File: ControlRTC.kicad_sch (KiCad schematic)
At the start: 33 parts, among them M1 Fan_4pin, SW1 SW_USER, SW2 SW_WIPE, U18 74LVC1G07, U19 74LVC1G07, U20 LP5569RTWR, U21 PCF85063AT, Y2 X32K768S301

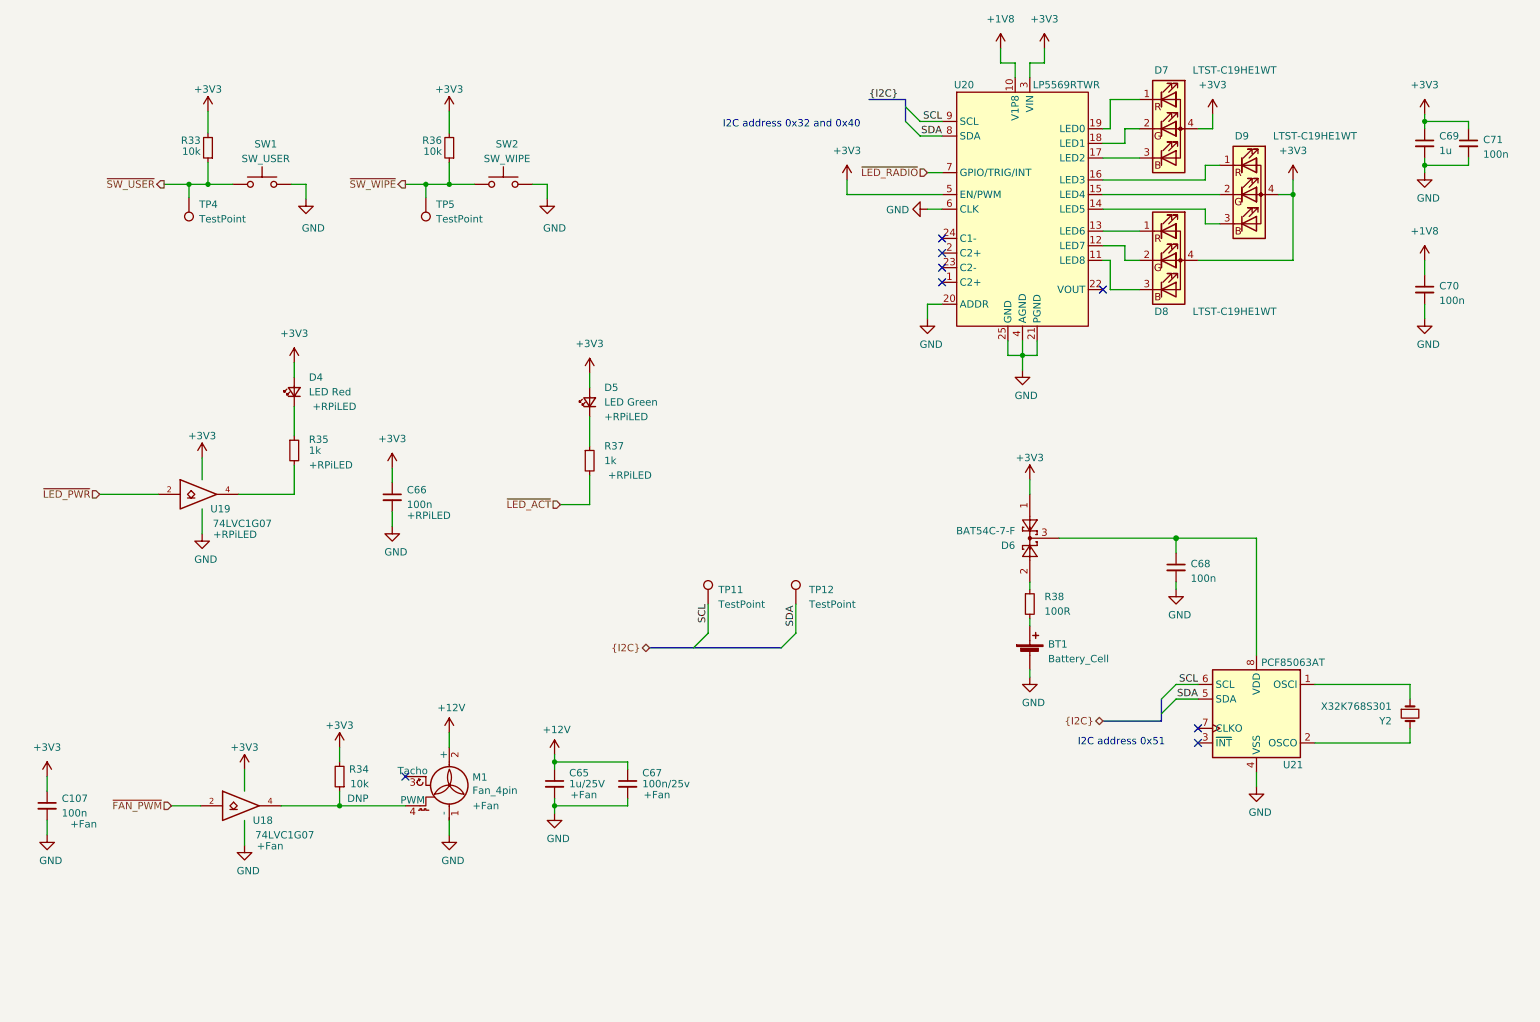
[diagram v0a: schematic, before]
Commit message: Update project files with latest KiCad 6 nightly
Signed-off-by: Stefan Agner <stefan@agner.ch>
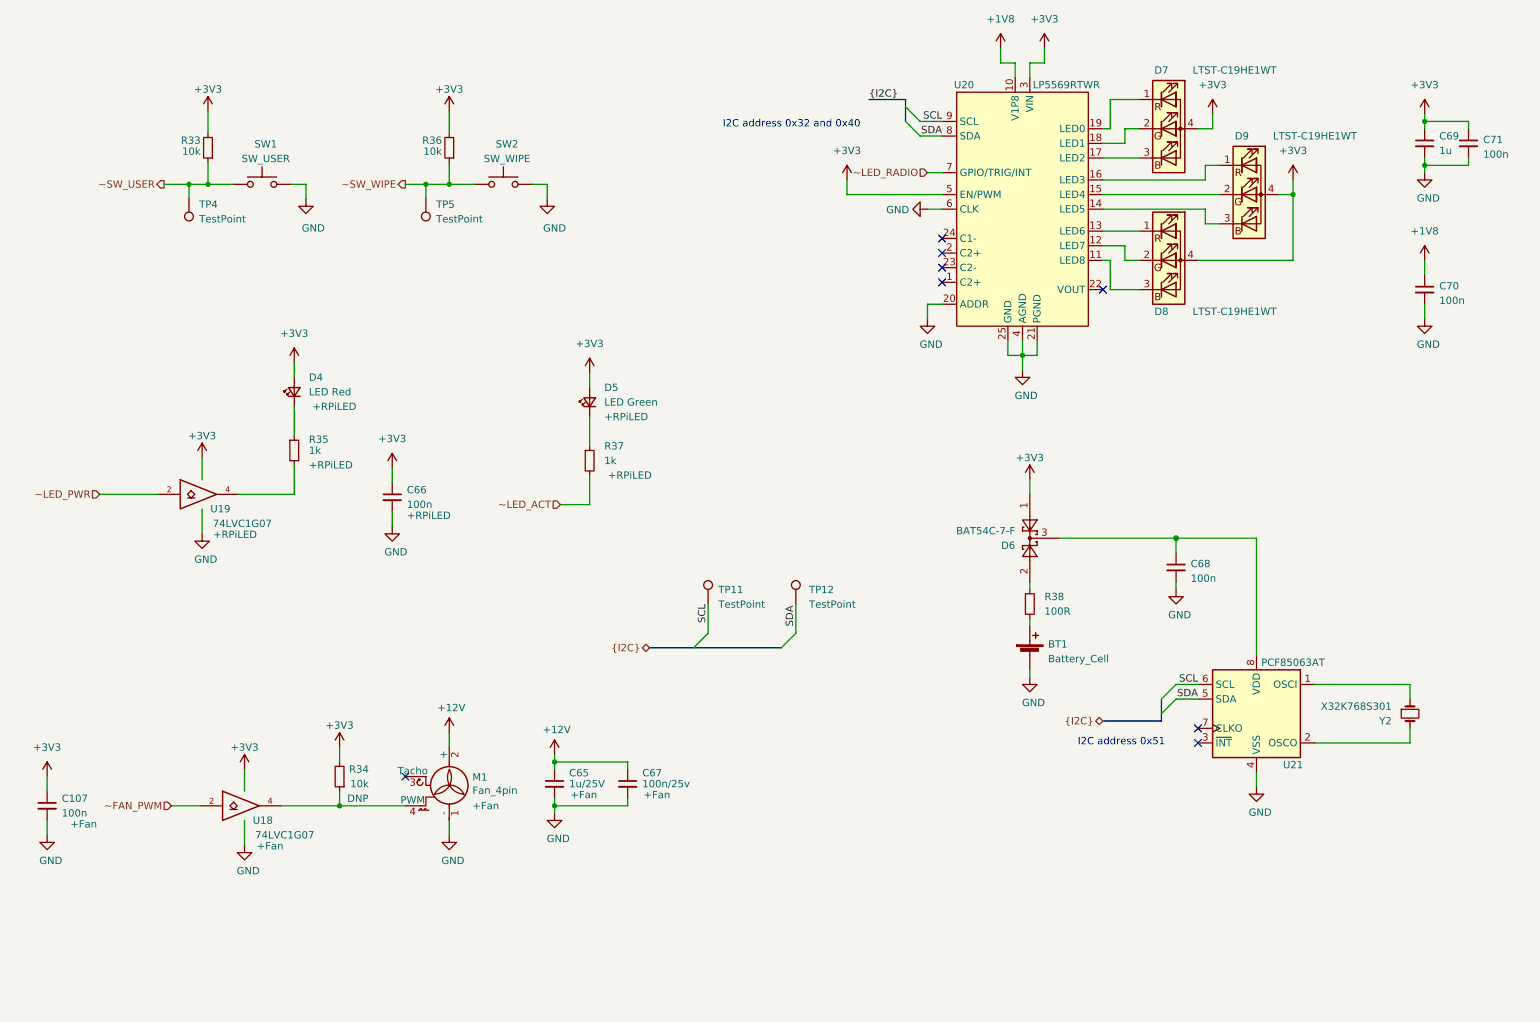
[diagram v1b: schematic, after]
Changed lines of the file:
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@@
-(kicad_sch (version 20210406) (generator eeschema)
+(kicad_sch (version 20210621) (generator eeschema)
   (paper "A4")
   (title_block

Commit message: Add second RTC symbol for alternative footprint
Add a second RTC symbol to support TSSOP-8 footprint besides the
existing 8-SOIC footprint.

Fixes: #29

Signed-off-by: Stefan Agner <stefan@agner.ch>
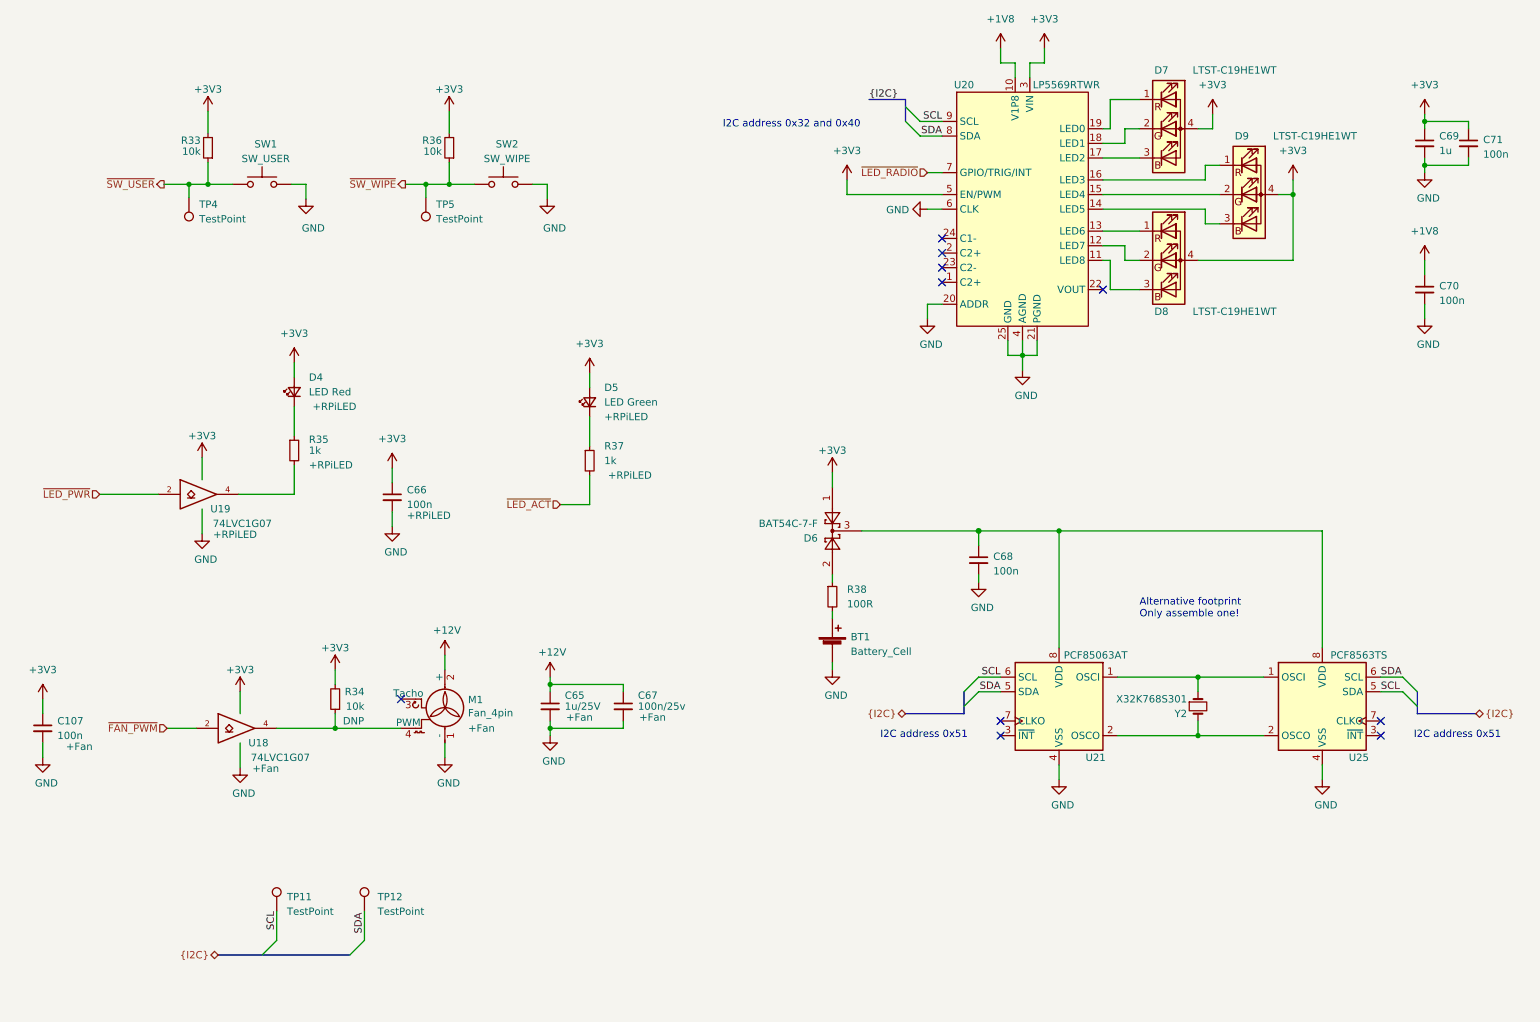
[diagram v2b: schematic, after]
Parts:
- added U25: PCF8563TS, Package_SO:MSOP-8_3x3mm_P0.65mm, symbol Timer_RTC:PCF8563TS
- U21: Config (none) -> DNP
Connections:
- net GND: now also U25.4 (VSS)
- net SCL: now also U25.5 (SDA)
- net SDA: now also U25.6 (SCL)
- net at U21.1 (OSCI), Y2.1: now also U25.1 (OSCI)
- net at U21.2 (OSCO), Y2.2: now also U25.2 (OSCO)
- net at C68.1, D6.3, U21.8 (VDD): now also U25.8 (VDD)
- net ~FAN_PWM renamed ~{FAN_PWM}
- net ~LED_ACT renamed ~{LED_ACT}
- net ~LED_PWR renamed ~{LED_PWR}
- net ~LED_RADIO renamed ~{LED_RADIO}
- net ~SW_USER renamed ~{SW_USER}
- net ~SW_WIPE renamed ~{SW_WIPE}
- no-connect marks 8 -> 10
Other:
- note added: "Alternative footprint Only assemble one!"
- moved on the sheet: BT1, C107, C65, C67, C68, D6, M1, R34, R38, TP11, TP12, U18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

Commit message: Deactivate RGB LEDs and use simple LED approach
Add Amber specific yellow LED as an additional status indicator.
Do not populate RGB LEDs and LP5569 LED controller.

Fixes: #32

Signed-off-by: Stefan Agner <stefan@agner.ch>
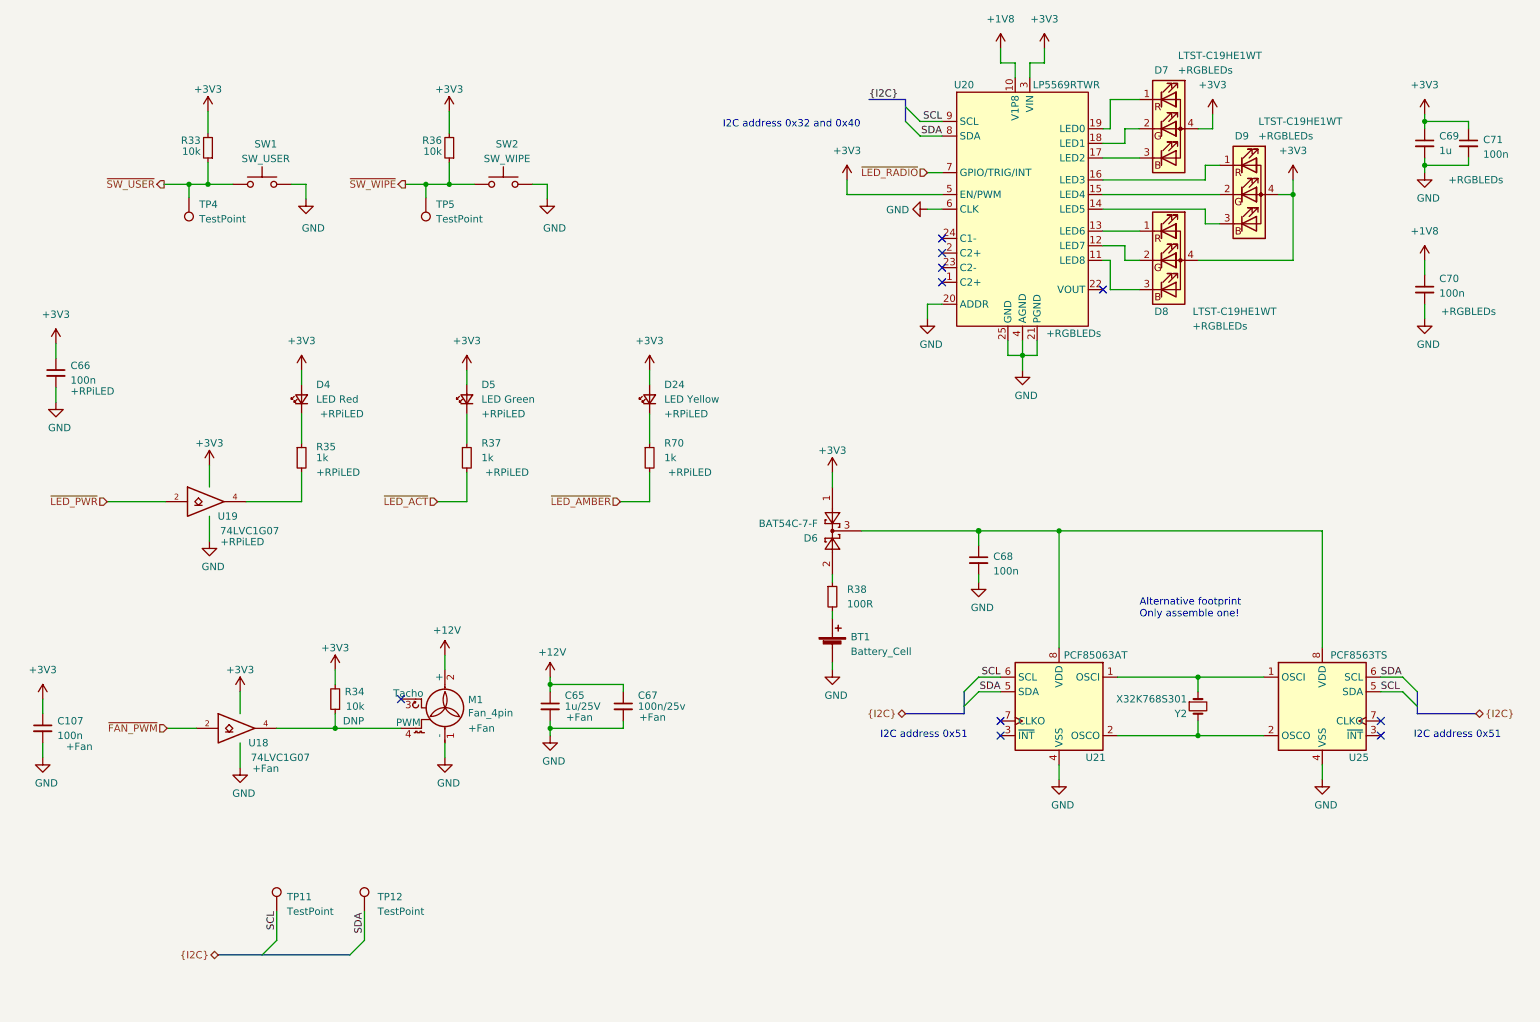
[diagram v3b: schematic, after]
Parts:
- added D24: LED Yellow, LED_SMD:LED_0603_1608Metric, symbol Device:LED_Small
- added R70: 1k, Resistor_SMD:R_0402_1005Metric, symbol Device:R_Small
- C69, C70, C71, D7, D8, D9, U20: Config (none) -> +RGBLEDs
- D4: Manufacturer Lite-On -> Everlight Elec; PartNumber LTST-C194KRKT -> 19-217/R6C-AL1M2VY/3T
- D5: Manufacturer Lite-On -> Everlight Elec; PartNumber LTST-C194TGKT -> 19-217/GHC-YR1S2/3T
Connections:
- net +3V3: now also D24.2 (A)
- new net: D24.1 (K), R70.1
- new net ~{LED_AMBER}: R70.2
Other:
- moved on the sheet: C66, D4, D5, R35, R37, U19

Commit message: Renmae LightBlue to Amber
Signed-off-by: Stefan Agner <stefan@agner.ch>
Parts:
- U20: symbol LightBlue:LP5569 -> Amber:LP5569
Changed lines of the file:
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@@
     (company "Nabu Casa")
     (comment 1 "www.nabucasa.com")
-    (comment 2 "Light Blue")
+    (comment 2 "Amber")
   )
   (junction (at 46.99 46.482) (diameter 0.9144) (color 0 0 0 0))
@@
     (pin "8")
   )
-  (symbol (lib_id "LightBlue:LP5569") (at 191.77 50.8 0) (unit 1)
+  (symbol (lib_id "Amber:LP5569") (at 191.77 50.8 0) (unit 1)
     (in_bom yes) (on_board yes)
     (property "Reference" "U20" (id 0) (at 181.61 29.21 0))
